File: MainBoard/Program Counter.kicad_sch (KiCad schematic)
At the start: 8 parts, among them U50 74ABT32, U51 74AHCT04, U52 IDT7381

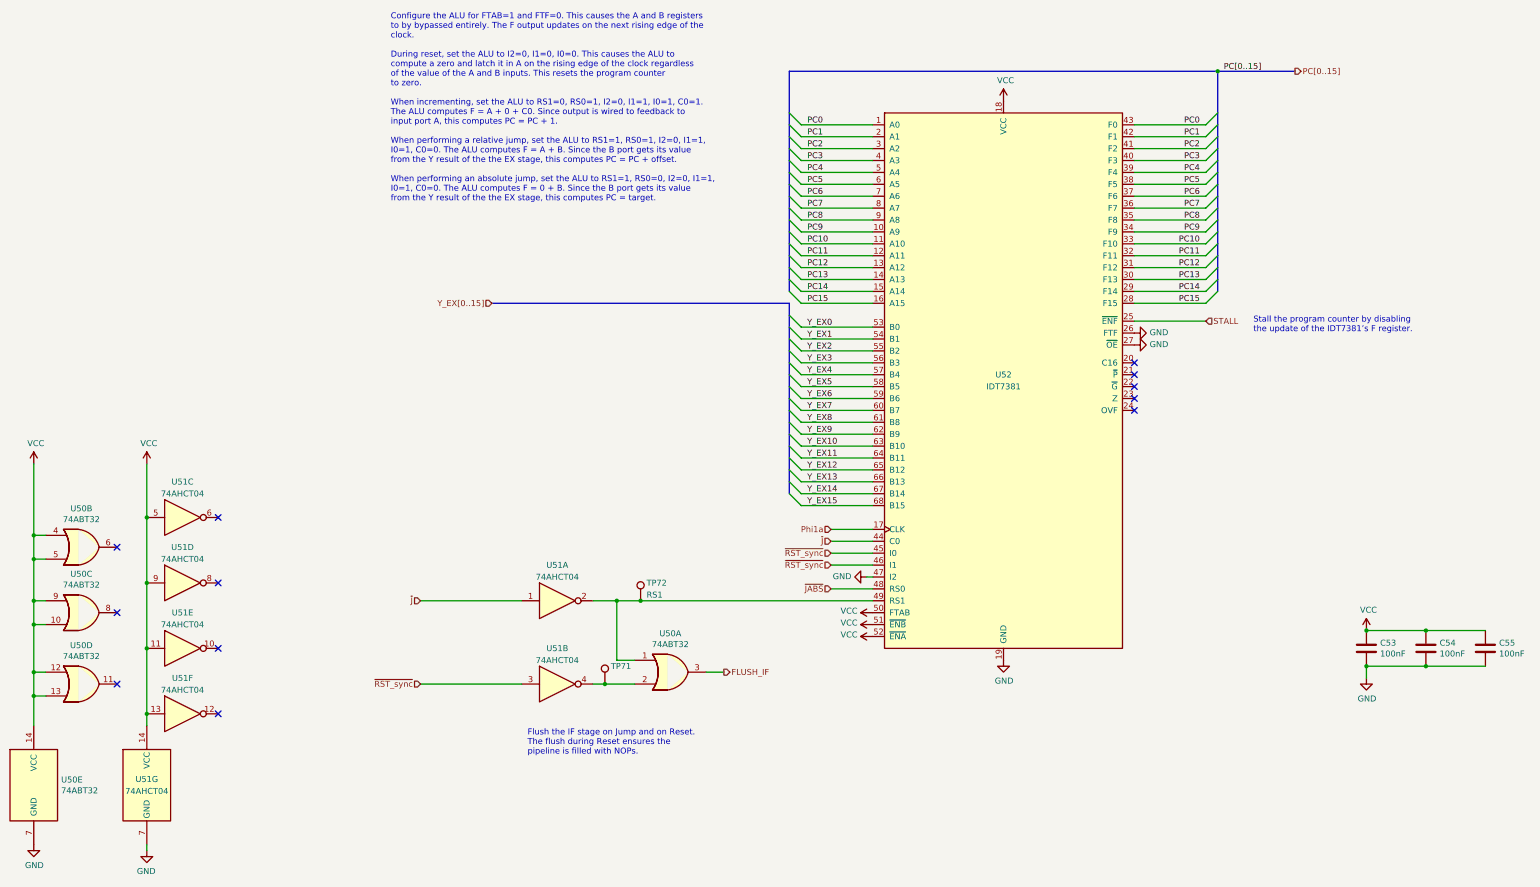
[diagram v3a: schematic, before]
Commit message: MainBoard: Update schematic to sync with MEMModule, Rev B
Unroute the PCB layout. Update the schematic to include changes from
revision B of MEMModule. This includes changes to put instruction ROM on
the PCB again.
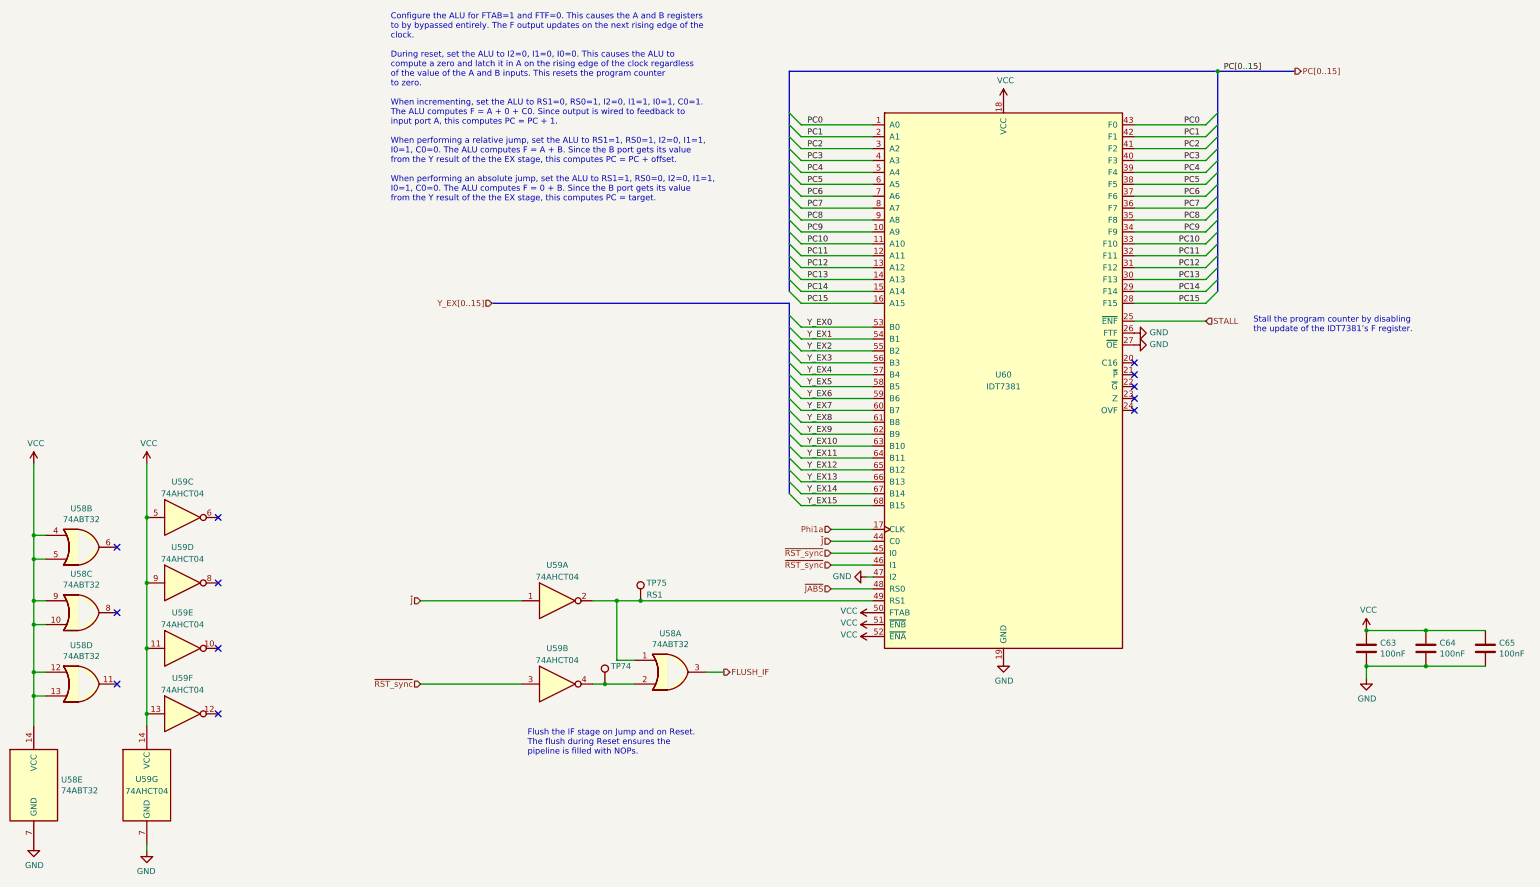
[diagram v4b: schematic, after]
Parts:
- renumbered C53 to C63, C54 to C64, C55 to C65, TP71 to TP74, TP72 to TP75, U50 to U58, U51 to U59, U52 to U60

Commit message: Update schematics for the MainBoard to include the ControleModule fix from 704c0dce
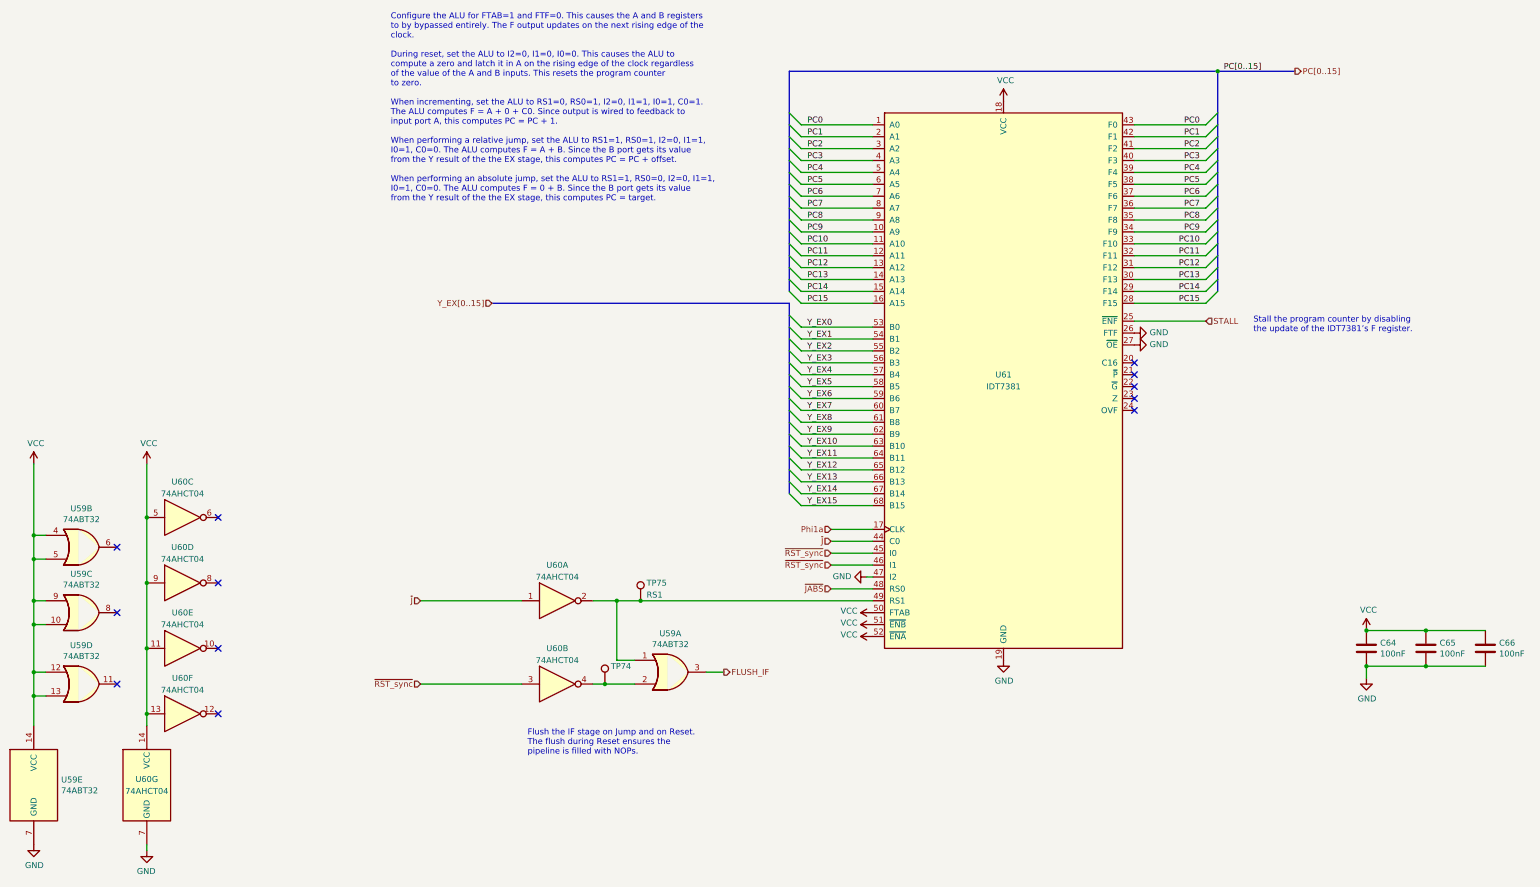
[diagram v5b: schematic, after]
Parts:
- renumbered C63 to C64, C64 to C65, C65 to C66, U58 to U59, U59 to U60, U60 to U61

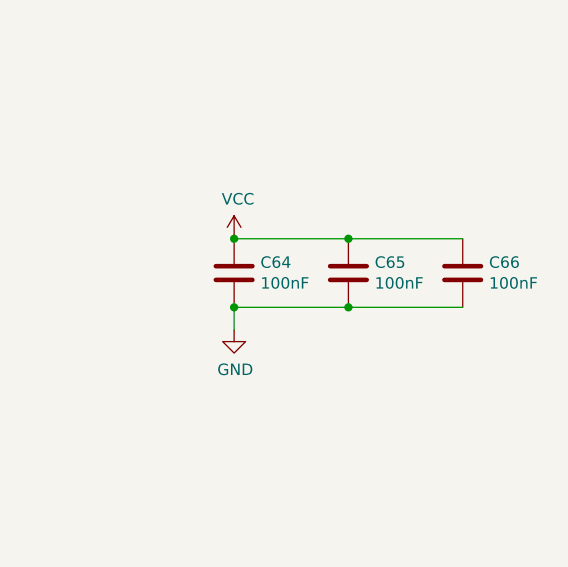
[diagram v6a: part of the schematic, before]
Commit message: MainBoard: Relabel capacitors from 100nF to 0.1uF
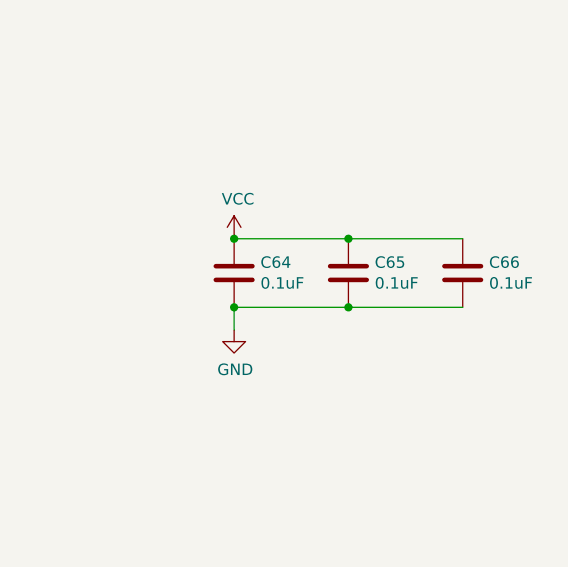
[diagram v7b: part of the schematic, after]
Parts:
- C64, C65, C66: value 100nF -> 0.1uF
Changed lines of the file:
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@@
       (effects (font (size 1.27 1.27)) (justify left))
     )
-    (property "Value" "100nF" (at 234.061 158.623 0)
+    (property "Value" "0.1uF" (at 234.061 158.623 0)
       (effects (font (size 1.27 1.27)) (justify left))
     )
@@
       (effects (font (size 1.27 1.27)) (justify left))
     )
-    (property "Value" "100nF" (at 246.761 158.623 0)
+    (property "Value" "0.1uF" (at 246.761 158.623 0)
       (effects (font (size 1.27 1.27)) (justify left))
     )
@@
       (effects (font (size 1.27 1.27)) (justify left))
     )
-    (property "Value" "100nF" (at 259.461 158.623 0)
-      (effects (font (size 1.27 1.27)) (justify left))
-    )
+    (property "Value" "0.1uF" (at 259.461 158.623 0)
+      (effects (font (size 1.27 1.27)) (justify left))
+    )

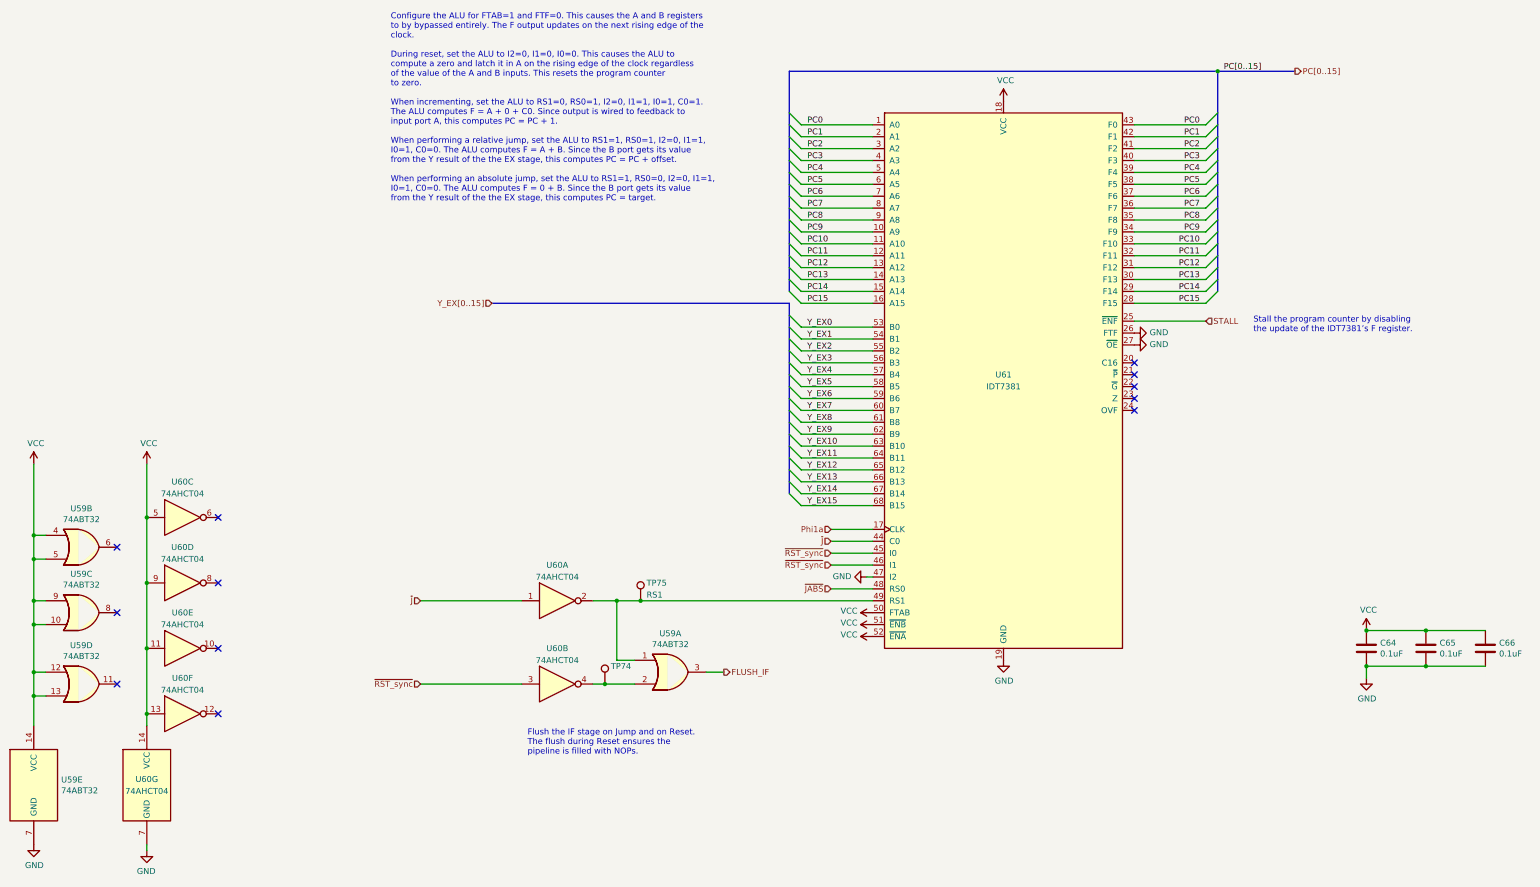
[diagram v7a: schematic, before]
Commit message: MainBoard: update schematic with latest changes to the clock
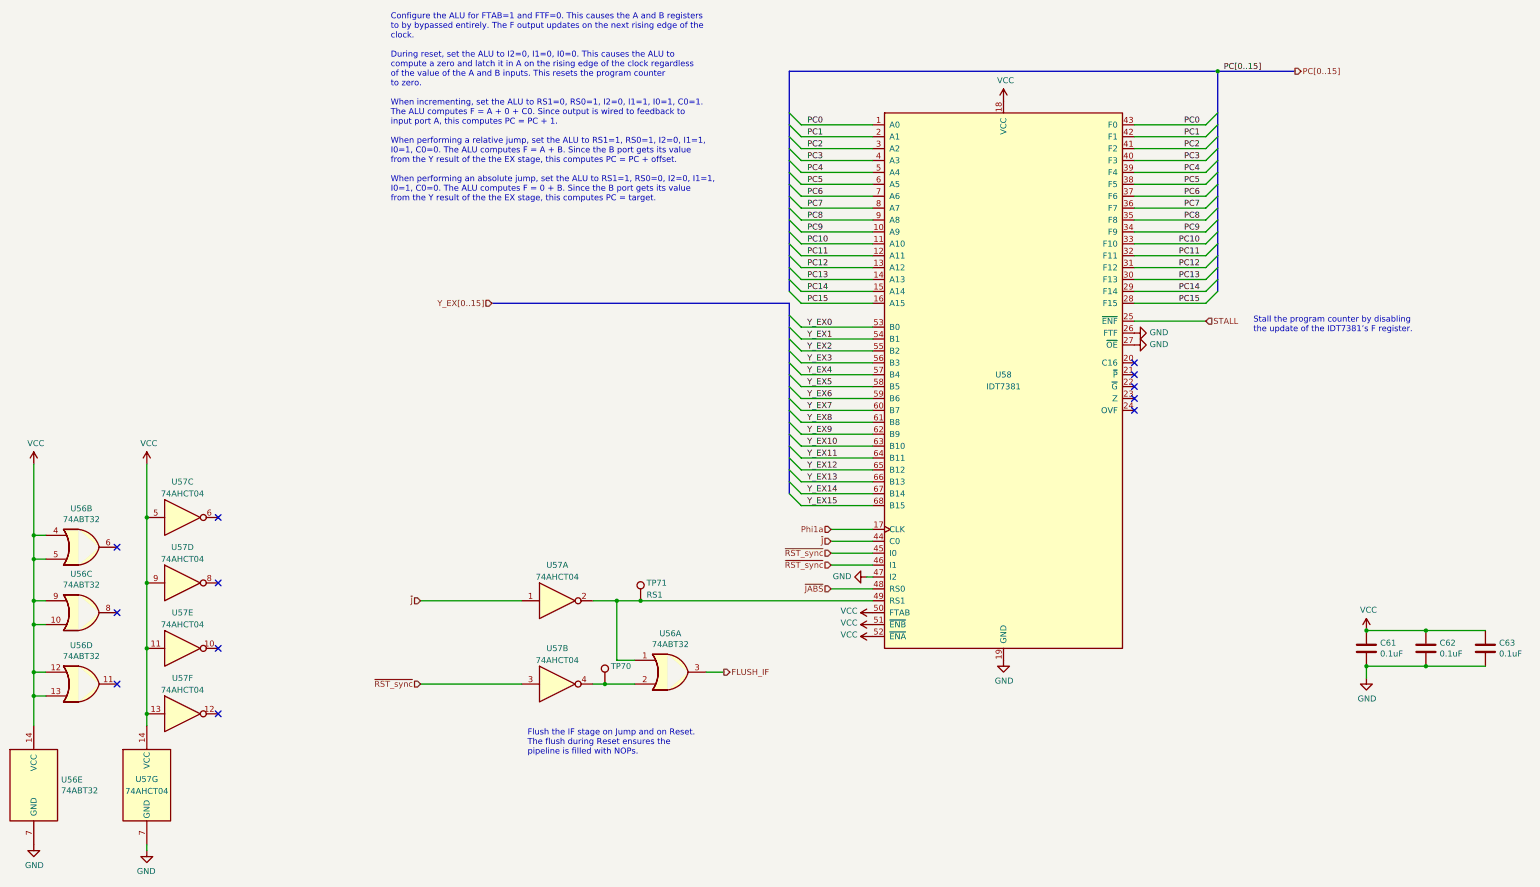
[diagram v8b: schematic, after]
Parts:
- renumbered C64 to C61, C65 to C62, C66 to C63, TP74 to TP70, TP75 to TP71, U59 to U56, U60 to U57, U61 to U58
